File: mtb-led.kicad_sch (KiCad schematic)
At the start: 57 parts, among them J7 AVR-ISP-6, J9 DEBUG, SW1 SW_Push, U1 ATmega328PB-A, U2 78M05, U3 TLC5940PWP, U4 TLC5940PWP, U5 MAX487E, Y1 14.7456 MHz

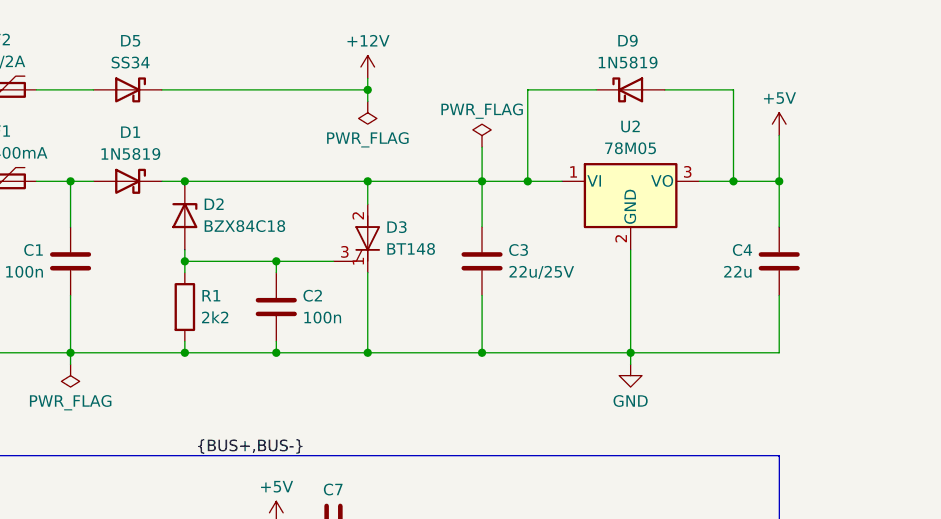
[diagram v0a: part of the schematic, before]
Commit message: Add capacitor to +12V.
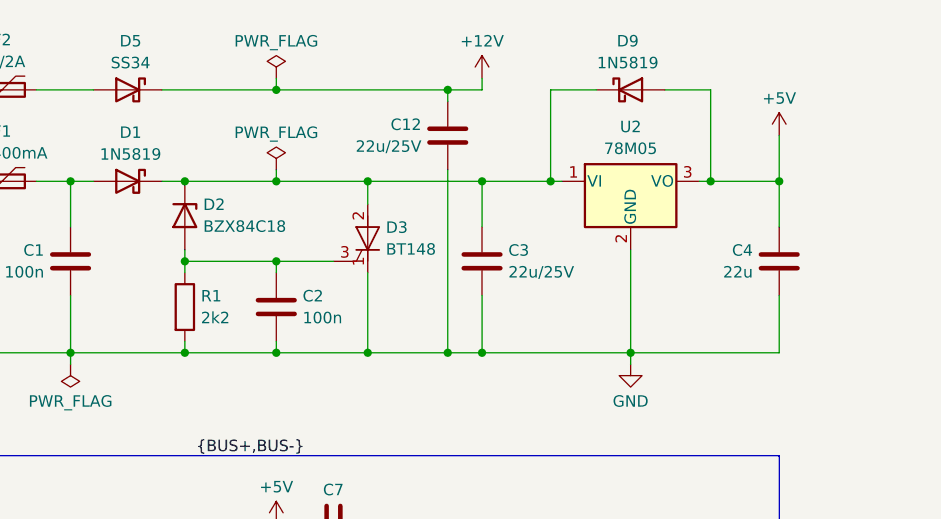
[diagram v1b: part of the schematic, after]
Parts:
- added C12: 22u/25V, Capacitor_SMD:C_0805_2012Metric, symbol Device:C
- D5: footprint Diode_SMD:D_SMA_Handsoldering -> Diode_SMD:D_SMA
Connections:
- net +12V: now also C12.1
- net GND: now also C12.2

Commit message: Add JLCPCB part numbers.
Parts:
- C1, C10, C11, C2, C7, C8, C9: LCSC (none) -> C49678
- C12, C3, C4: LCSC (none) -> C45783
- C5, C6: LCSC (none) -> C1804
- D1, D9: LCSC (none) -> C191023
- D2: JLCPCB_CORRECTION (none) -> 0;0;180; LCSC (none) -> C896938
- D3: JLCPCB_CORRECTION (none) -> 0;0;180; LCSC (none) -> C256433
- D4: LCSC (none) -> C2827658
- D5: LCSC (none) -> C8678
- D6, D7, D8, F1, F2, H1, H2, H3, H4, J1, J2, J3, J4, J5, J6, J7, J8, J9, JP1, SW1, TP1, TP2, TP3, TP4, U5, Y1: JLCPCB_IGNORE (none) -> true
- R1, R8: LCSC (none) -> C17520
- R10, R2, R5, R7, R9: LCSC (none) -> C17414
- R3, R4: LCSC (none) -> C17604
- R6: LCSC (none) -> C17513
- U1: JLCPCB_CORRECTION (none) -> 0;0;-90; LCSC (none) -> C132230
- U2: JLCPCB_CORRECTION (none) -> -1.8;0;0; LCSC (none) -> C58069
- U3, U4: JLCPCB_CORRECTION (none) -> 0;0;-90; LCSC (none) -> C181653

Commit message: Add vias.
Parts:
- Y1: footprint Crystal:Crystal_HC49-U_Vertical -> Crystal:Crystal_HC49-4H_Vertical
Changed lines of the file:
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@@
 			)
 		)
-		(property "Footprint" "Crystal:Crystal_HC49-U_Vertical"
+		(property "Footprint" "Crystal:Crystal_HC49-4H_Vertical"
 			(at 264.16 60.96 0)
 			(effects

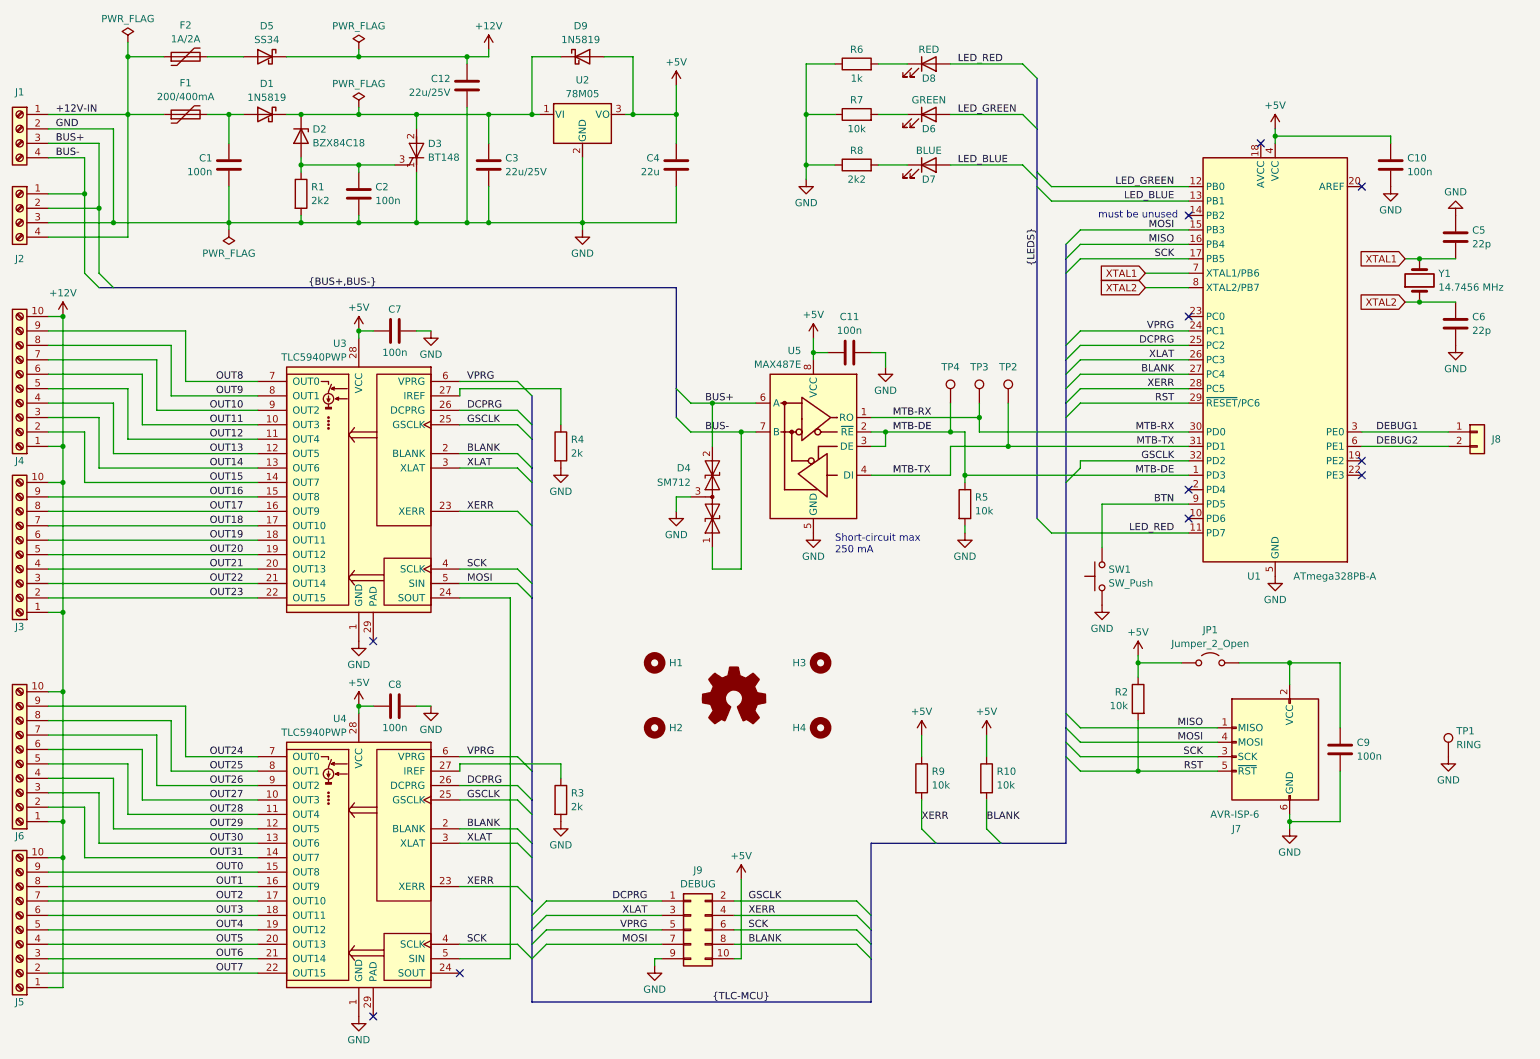
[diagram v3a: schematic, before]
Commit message: Rewire MCU connection (v1.1).
* Use OCR1A/B pins for XLAT & BLANK. HW timer output required.
* Reconnect BLUE LED to different PIN.
* Add MISO TLC->ATmega.
* Use SPI1 for TLS connection, SPI0 for programming.
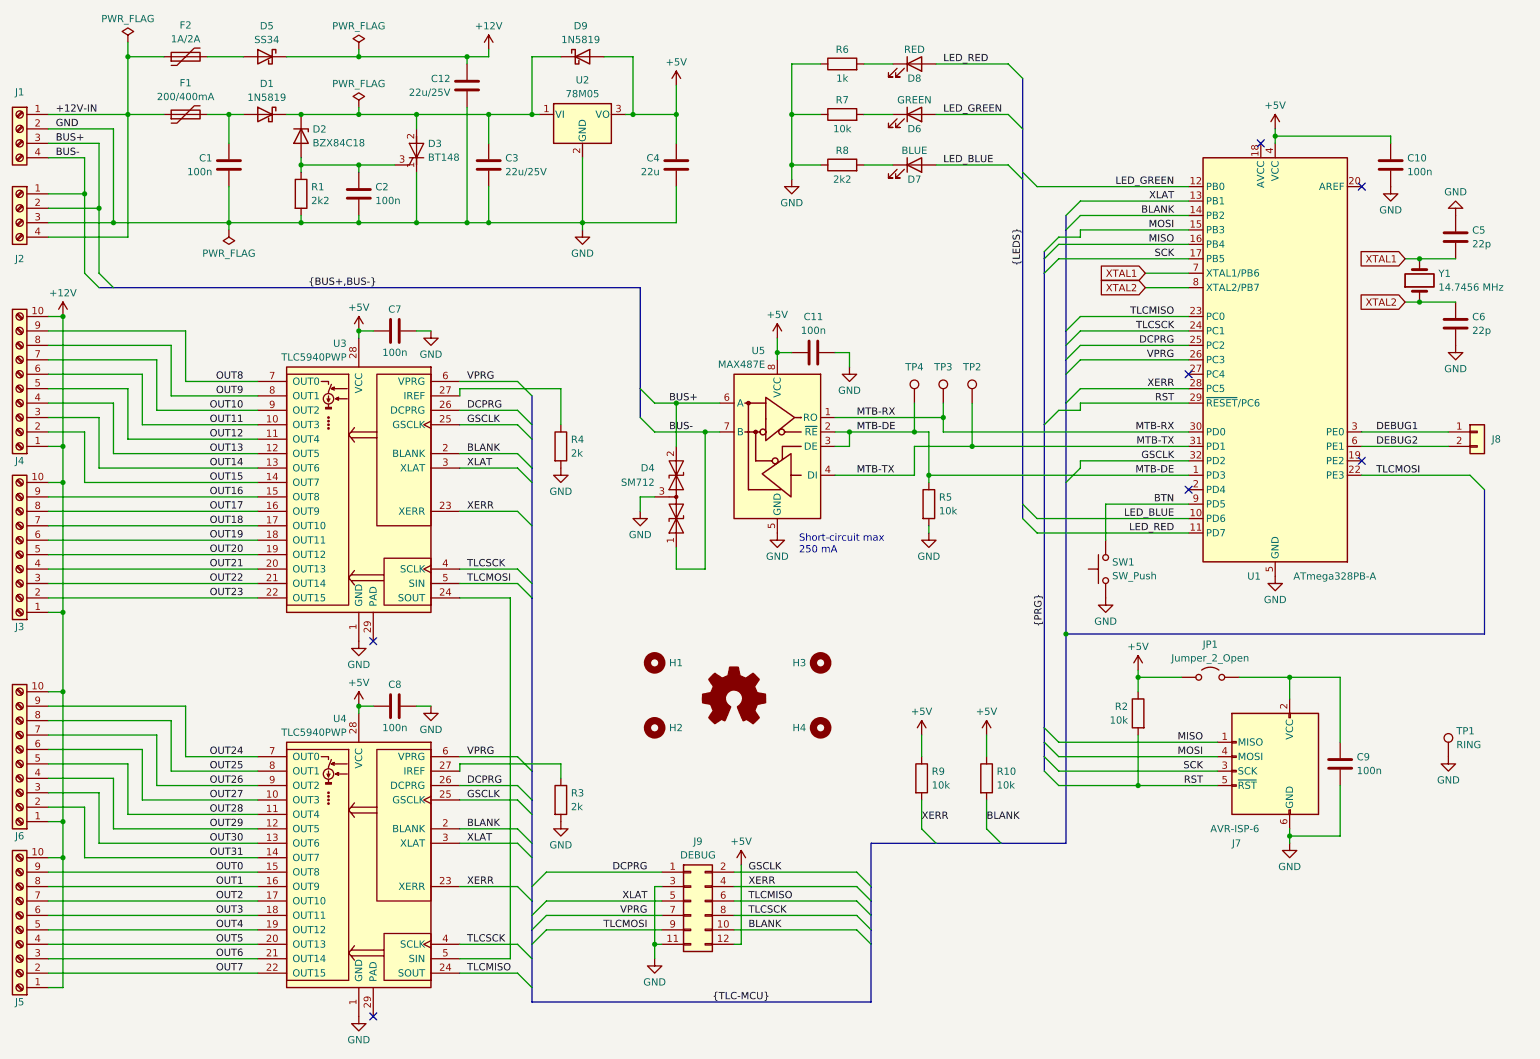
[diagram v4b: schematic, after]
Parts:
- J9: footprint Connector_PinHeader_2.54mm:PinHeader_2x05_P2.54mm_Vertical -> Connector_PinHeader_2.54mm:PinHeader_2x06_P2.54mm_Vertical; symbol Connector_Generic:Conn_02x05_Odd_Even -> Connector_Generic:Conn_02x06_Odd_Even
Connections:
- net +5V: now also J9.12 (Pin_12); no longer J9.10 (Pin_10)
- net BLANK: now also J9.10 (Pin_10), U1.14 (PB2); no longer J9.8 (Pin_8), U1.27 (PC4)
- net GND: now also J9.11 (Pin_11), J9.3 (Pin_3); no longer J9.9 (Pin_9)
- net LED_BLUE: now also U1.10 (PD6); no longer U1.13 (PB1)
- net MOSI: no longer J9.7 (Pin_7), U3.5 (SIN)
- net SCK: no longer J9.6 (Pin_6), U3.4 (SCLK), U4.4 (SCLK)
- net VPRG: now also J9.7 (Pin_7), U1.26 (PC3); no longer J9.5 (Pin_5), U1.24 (PC1)
- net XLAT: now also J9.5 (Pin_5), U1.13 (PB1); no longer J9.3 (Pin_3), U1.26 (PC3)
- net TLCMOSI: now reaches U1.22 (PE3)
- net TLCMOSI: now also J9.9 (Pin_9), U3.5 (SIN)
- net TLCMISO: now reaches U1.23 (PC0)
- net TLCMISO: now also J9.6 (Pin_6), U4.24 (SOUT)
- new net TLCSCK: J9.8 (Pin_8), U1.24 (PC1), U3.4 (SCLK), U4.4 (SCLK)
- no-connect marks 11 -> 7
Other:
- note removed: "must be unused"
- moved on the sheet: C11, C9, D4, D6, D7, D8, J7, JP1, R2, R5, R6, R7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

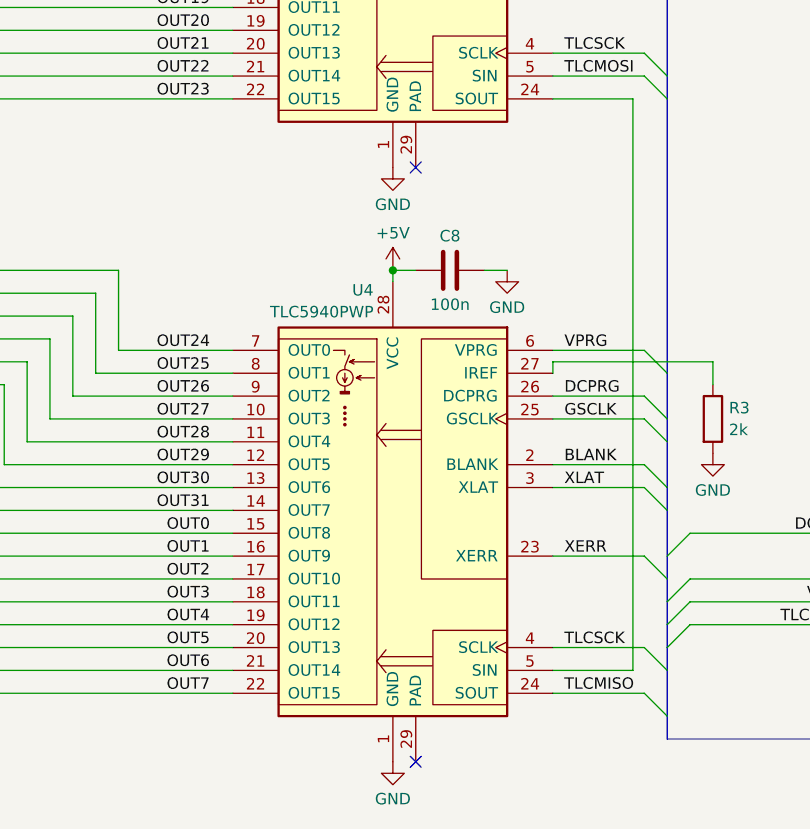
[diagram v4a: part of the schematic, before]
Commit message: Connect TLC5940 thermal pad to GND.
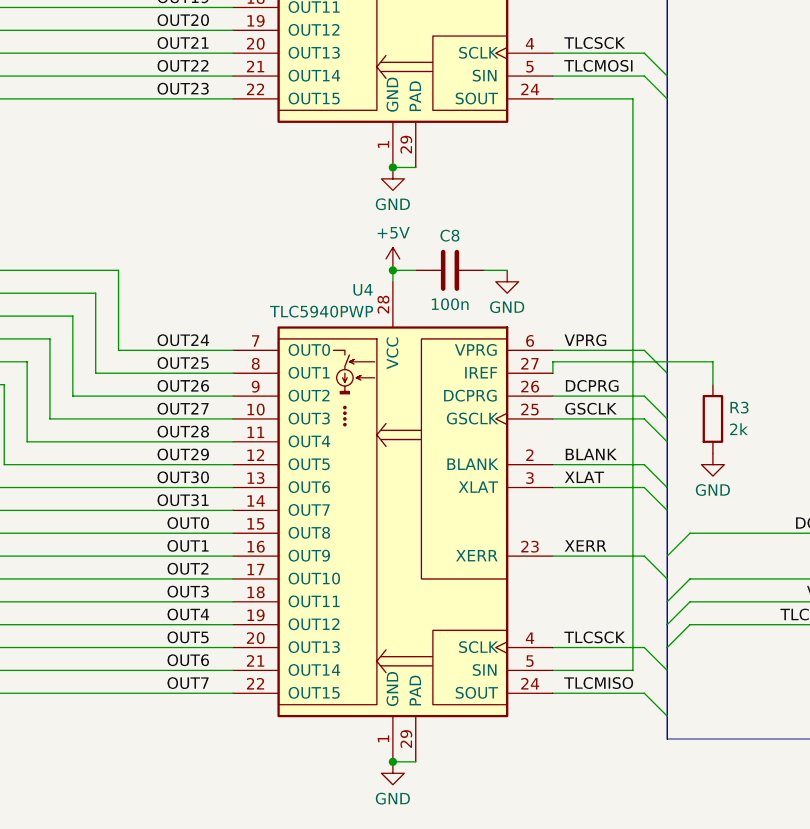
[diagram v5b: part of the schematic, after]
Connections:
- net GND: now also U3.29 (PAD), U4.29 (PAD)
- no-connect marks 7 -> 5
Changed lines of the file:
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@@
+	)
+	(junction
+		(at 77.47 124.46)
+		(diameter 0)
+		(color 0 0 0 0)
 	)
 	(junction
@@
 		(color 0 0 0 0)
 	)
-	(no_connect
-		(at 80.01 190.5)
+	(junction
+		(at 77.47 190.5)
+		(diameter 0)
+		(color 0 0 0 0)
 	)
 	(no_connect
@@
 	)
 	(no_connect
-		(at 80.01 124.46)
-	)
-	(no_connect
 		(at 236.22 36.83)
 	)
@@
 	(wire
 		(pts
+			(xy 77.47 124.46) (xy 80.01 124.46)
+		)
+		(stroke
+			(width 0)
+			(type default)
+		)
+	)
+	(wire
+		(pts
 			(xy 163.83 87.63) (xy 161.29 87.63)
 		)
@@
 		)
 		(stroke
+			(width 0)
+			(type default)
+		)
+	)
+	(wire
+		(pts
+			(xy 77.47 190.5) (xy 80.01 190.5)
+		)
+		(stroke

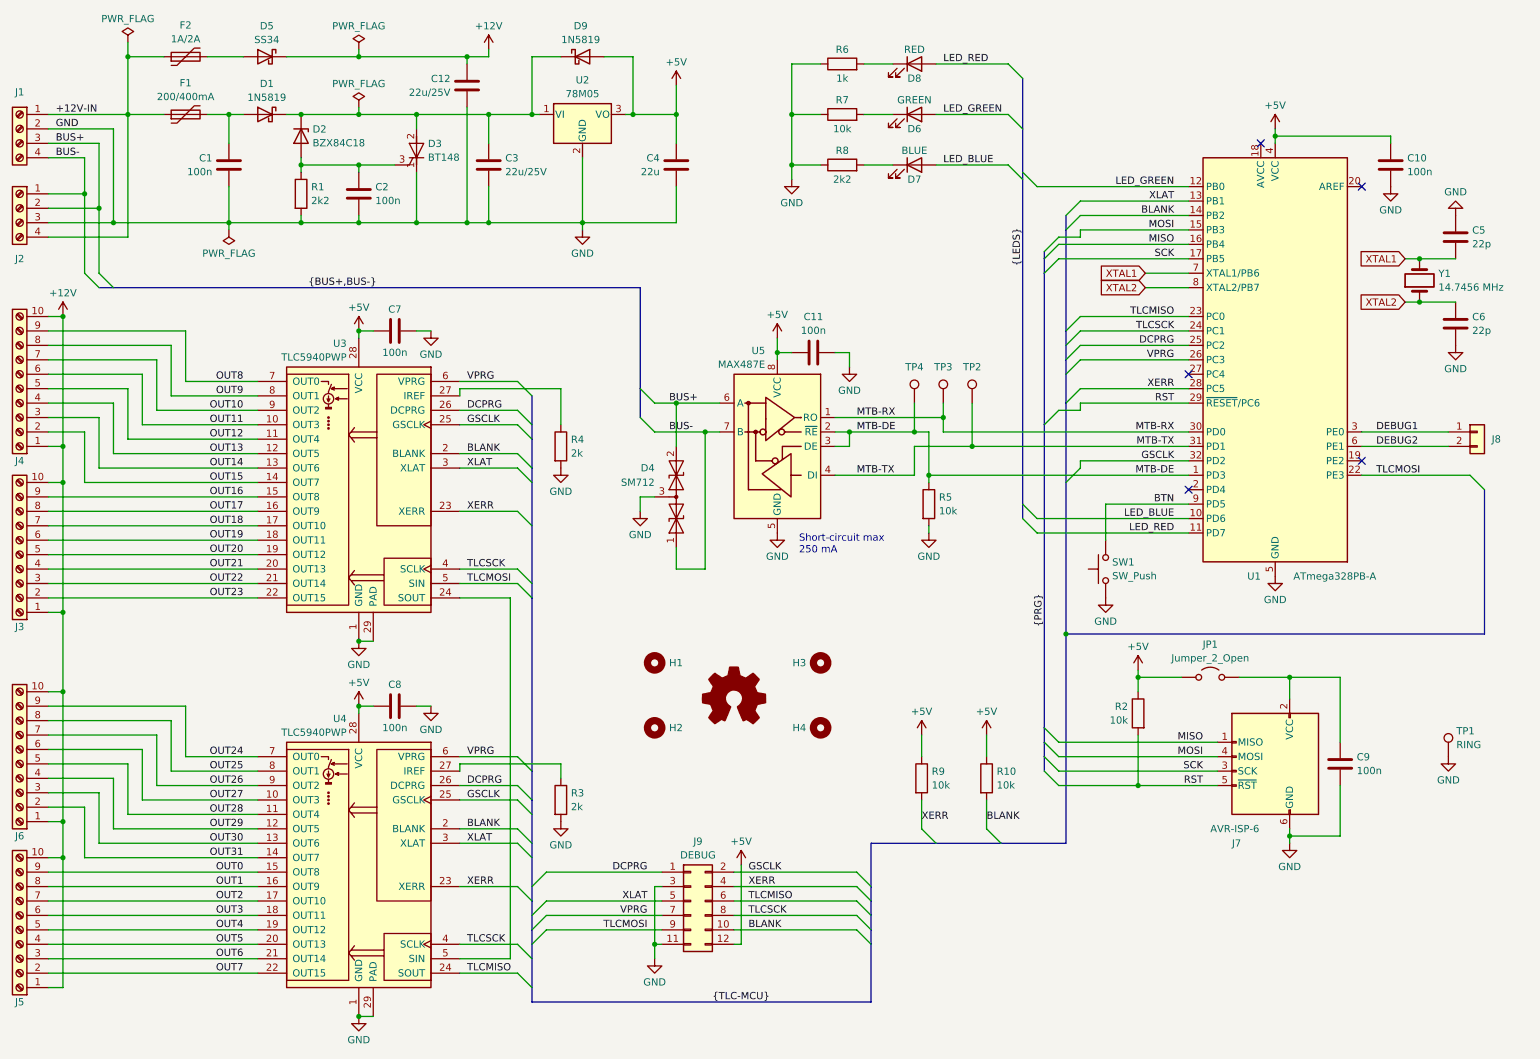
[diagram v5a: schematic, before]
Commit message: Remove XERR signal.
It is not used.
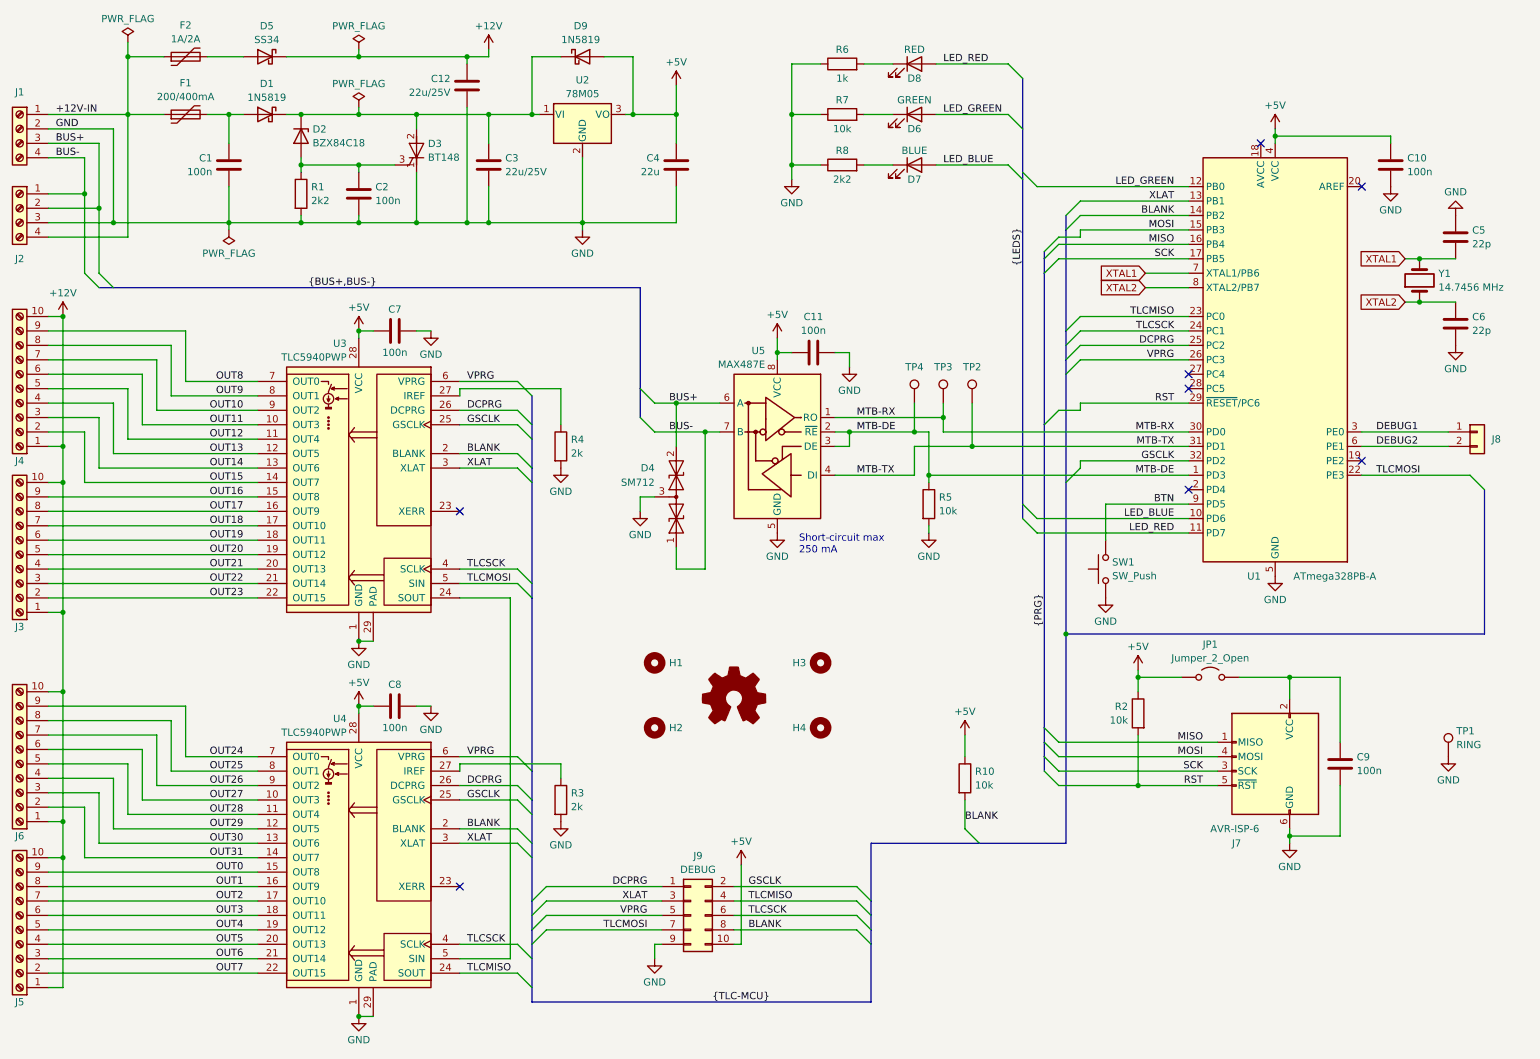
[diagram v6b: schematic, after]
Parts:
- removed R9: 10k, Resistor_SMD:R_0805_2012Metric, symbol Device:R
- J9: footprint Connector_PinHeader_2.54mm:PinHeader_2x06_P2.54mm_Vertical -> Connector_PinHeader_2.54mm:PinHeader_2x05_P2.54mm_Vertical; symbol Connector_Generic:Conn_02x06_Odd_Even -> Connector_Generic:Conn_02x05_Odd_Even
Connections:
- net +5V: now also J9.10 (Pin_10); no longer J9.12 (Pin_12)
- net BLANK: now also J9.8 (Pin_8); no longer J9.10 (Pin_10)
- net GND: now also J9.9 (Pin_9); no longer J9.11 (Pin_11), J9.3 (Pin_3)
- net TLCMISO: now also J9.4 (Pin_4); no longer J9.6 (Pin_6)
- net TLCMOSI: now also J9.7 (Pin_7); no longer J9.9 (Pin_9)
- net TLCSCK: now also J9.6 (Pin_6); no longer J9.8 (Pin_8)
- net VPRG: now also J9.5 (Pin_5); no longer J9.7 (Pin_7)
- net XLAT: now also J9.3 (Pin_3); no longer J9.5 (Pin_5)
- removed net XERR: J9.4 (Pin_4), U1.28 (PC5), U3.23 (XERR), U4.23 (XERR)
- no-connect marks 5 -> 8
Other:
- moved on the sheet: R10
